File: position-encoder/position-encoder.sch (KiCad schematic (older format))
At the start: 9 parts, among them J1 Conn_01x04_Male, U1 TLE4905L, U2 TLE4905L

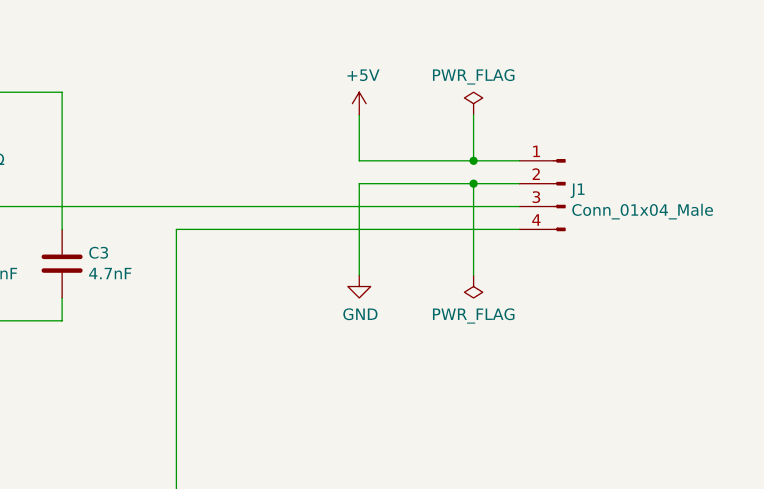
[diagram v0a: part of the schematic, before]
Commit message: Add PCB for position encoder
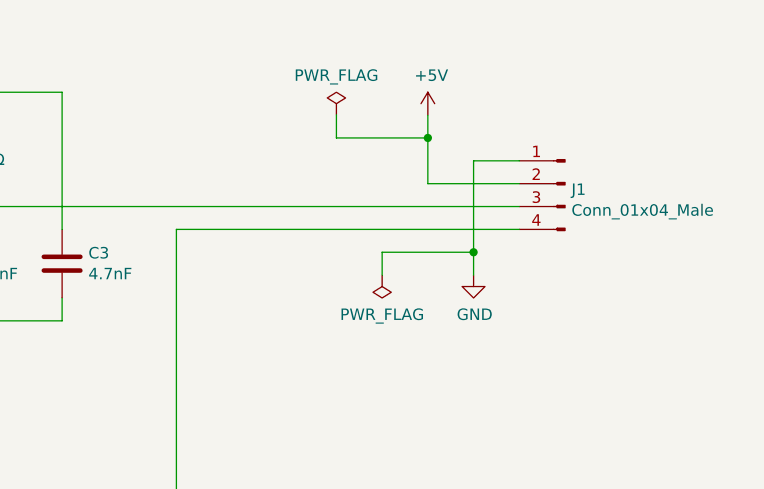
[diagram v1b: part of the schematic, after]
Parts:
- U1, U2: footprint (none) -> earth-rover-custom-footprints:PG-SSO-3-2_W2.54mm_Horizontal_Down
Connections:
- net +5V: now also J1.2 (Pin_2); no longer J1.1 (Pin_1)
- net GND: now also J1.1 (Pin_1); no longer J1.2 (Pin_2)
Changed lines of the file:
@@
 encoding utf-8
 Sheet 1 1
-Title "Position Encoder for RC Volvo C202"
+Title "Position Encoder for Earth Rover"
 Date "2019-11-11"
 Rev "1"
@@
 F 0 "U1" H 2473 3046 50  0000 R CNN
 F 1 "TLE4905L" H 2473 2955 50  0000 R CNN
-F 2 "" H 2700 3000 50  0001 C CNN
+F 2 "earth-rover-custom-footprints:PG-SSO-3-2_W2.54mm_Horizontal_Down" H 2700 3000 50  0001 C CNN
 F 3 "https://www.infineon.com/cms/en/product/sensor/magnetic-sensors/magnetic-position-sensors/hall-switches/tle4905l/" H 2700 3000 50  0001 C CNN
 	1    2700 3000
@@
 F 0 "U2" H 2473 5046 50  0000 R CNN
 F 1 "TLE4905L" H 2473 4955 50  0000 R CNN
-F 2 "" H 2700 5000 50  0001 C CNN
+F 2 "earth-rover-custom-footprints:PG-SSO-3-2_W2.54mm_Horizontal_Down" H 2700 5000 50  0001 C CNN
 F 3 "https://www.infineon.com/cms/en/product/sensor/magnetic-sensors/magnetic-position-sensors/hall-switches/tle4905l/" H 2700 5000 50  0001 C CNN
 	1    2700 5000
@@
 L power:GND #PWR0105
 U 1 1 5DCC09FC
-P 5000 3300
-F 0 "#PWR0105" H 5000 3050 50  0001 C CNN
-F 1 "GND" H 5005 3127 50  0000 C CNN
-F 2 "" H 5000 3300 50  0001 C CNN
-F 3 "" H 5000 3300 50  0001 C CNN
-	1    5000 3300
+P 5500 3300
+F 0 "#PWR0105" H 5500 3050 50  0001 C CNN
+F 1 "GND" H 5505 3127 50  0000 C CNN
+F 2 "" H 5500 3300 50  0001 C CNN
+F 3 "" H 5500 3300 50  0001 C CNN
+	1    5500 3300
 	1    0    0    -1
 $EndComp
@@
 L power:+5V #PWR0106
 U 1 1 5DCC1747
-P 5000 2600
-F 0 "#PWR0106" H 5000 2450 50  0001 C CNN
-F 1 "+5V" H 5015 2773 50  0000 C CNN
-F 2 "" H 5000 2600 50  0001 C CNN
-F 3 "" H 5000 2600 50  0001 C CNN
-	1    5000 2600
+P 5300 2600
+F 0 "#PWR0106" H 5300 2450 50  0001 C CNN
+F 1 "+5V" H 5315 2773 50  0000 C CNN
+F 2 "" H 5300 2600 50  0001 C CNN
+F 3 "" H 5300 2600 50  0001 C CNN
+	1    5300 2600
 	1    0    0    -1
 $EndComp
@@
 L power:PWR_FLAG #FLG0101
 U 1 1 5DD0D13F
-P 5500 2600
-F 0 "#FLG0101" H 5500 2675 50  0001 C CNN
-F 1 "PWR_FLAG" H 5500 2773 50  0000 C CNN
-F 2 "" H 5500 2600 50  0001 C CNN
-F 3 "~" H 5500 2600 50  0001 C CNN
-	1    5500 2600
+P 4900 2600
+F 0 "#FLG0101" H 4900 2675 50  0001 C CNN
+F 1 "PWR_FLAG" H 4900 2773 50  0000 C CNN
+F 2 "" H 4900 2600 50  0001 C CNN
+F 3 "~" H 4900 2600 50  0001 C CNN
+	1    4900 2600
 	1    0    0    -1
 $EndComp
@@
 L power:PWR_FLAG #FLG0102
 U 1 1 5DD0E731
-P 5500 3300
-F 0 "#FLG0102" H 5500 3375 50  0001 C CNN
-F 1 "PWR_FLAG" H 5500 3473 50  0000 C CNN
-F 2 "" H 5500 3300 50  0001 C CNN
-F 3 "~" H 5500 3300 50  0001 C CNN
-	1    5500 3300
+P 5100 3300
+F 0 "#FLG0102" H 5100 3375 50  0001 C CNN
+F 1 "PWR_FLAG" H 5100 3473 50  0000 C CNN
+F 2 "" H 5100 3300 50  0001 C CNN
+F 3 "~" H 5100 3300 50  0001 C CNN
+	1    5100 3300
 	1    0    0    1
 $EndComp
@@
 	4200 3100 5700 3100
 Wire Wire Line
-	5000 3300 5000 2900
-Wire Wire Line
-	5000 2900 5500 2900
-Wire Wire Line
-	5000 2600 5000 2800
-Wire Wire Line
-	5000 2800 5500 2800
-Wire Wire Line
-	5500 2600 5500 2800
-Connection ~ 5500 2800
-Wire Wire Line
-	5500 2800 5700 2800
-Wire Wire Line
-	5500 3300 5500 2900
-Connection ~ 5500 2900
-Wire Wire Line
-	5500 2900 5700 2900
+	5700 2800 5500 2800
+Wire Wire Line
+	5500 2800 5500 3200
+Wire Wire Line
+	5100 3300 5100 3200
+Wire Wire Line
+	5100 3200 5500 3200
+Connection ~ 5500 3200
+Wire Wire Line
+	5500 3200 5500 3300
+Wire Wire Line
+	5300 2600 5300 2700
+Wire Wire Line
+	5300 2900 5700 2900
+Wire Wire Line
+	4900 2600 4900 2700
+Wire Wire Line
+	4900 2700 5300 2700
+Connection ~ 5300 2700
+Wire Wire Line
+	5300 2700 5300 2900
 $EndSCHEMATC

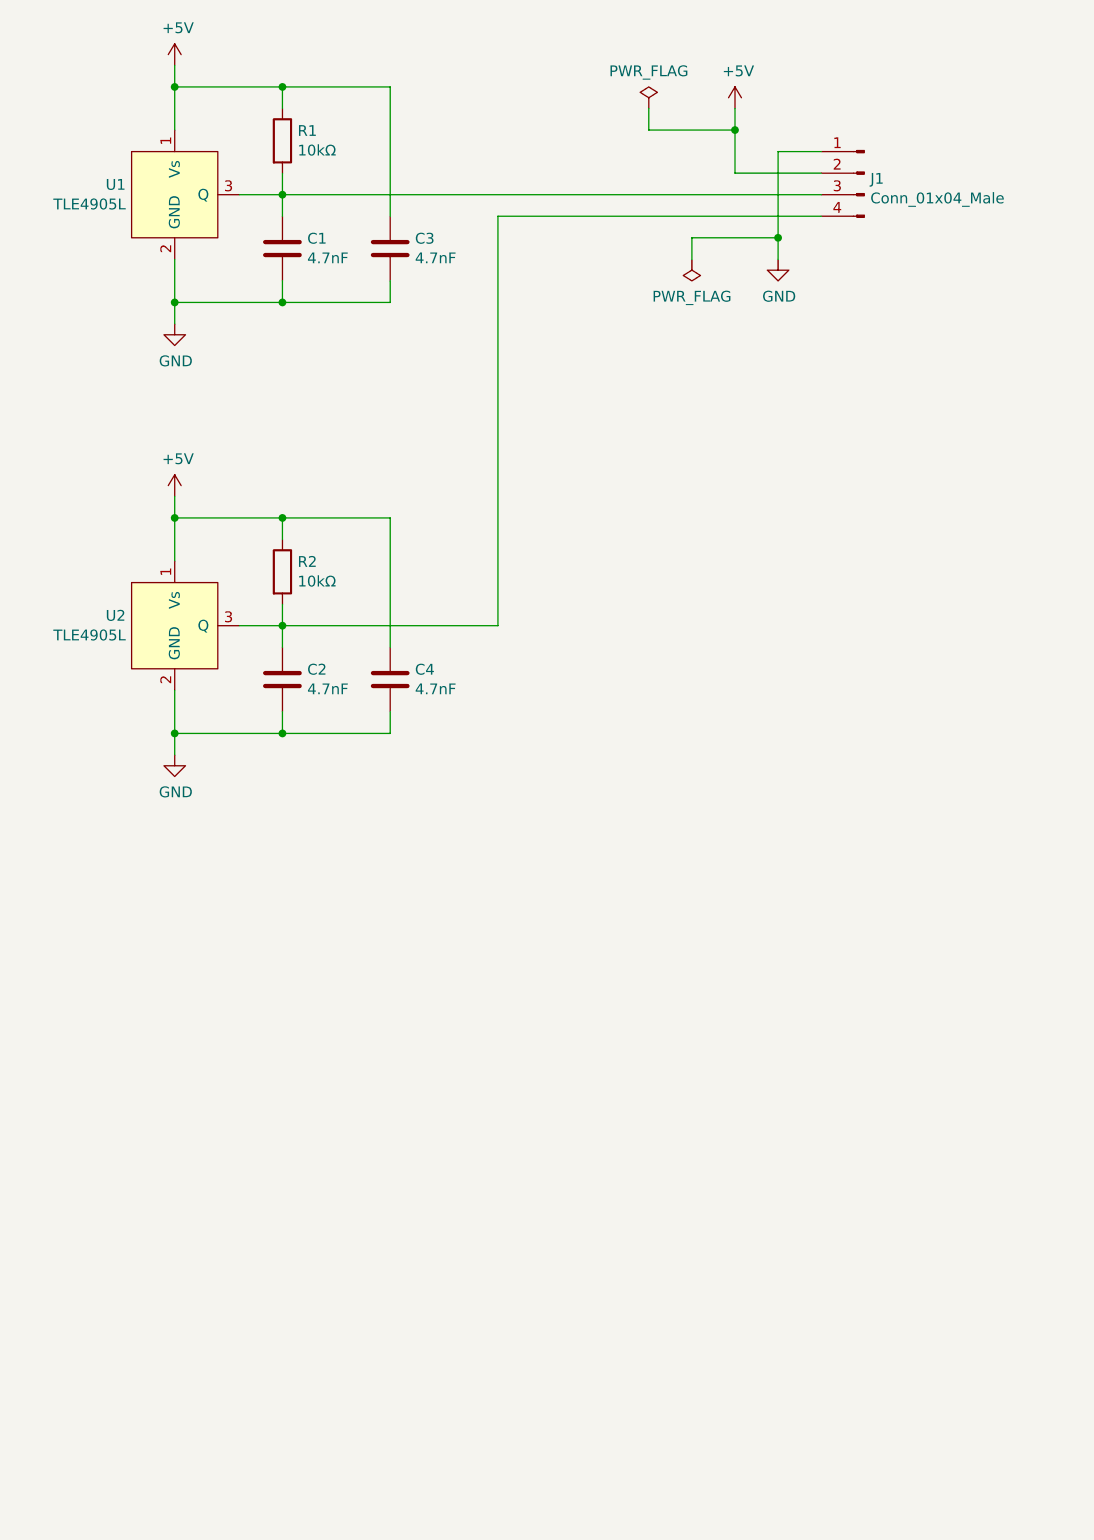
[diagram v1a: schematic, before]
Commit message: Add custom KiCad page layout
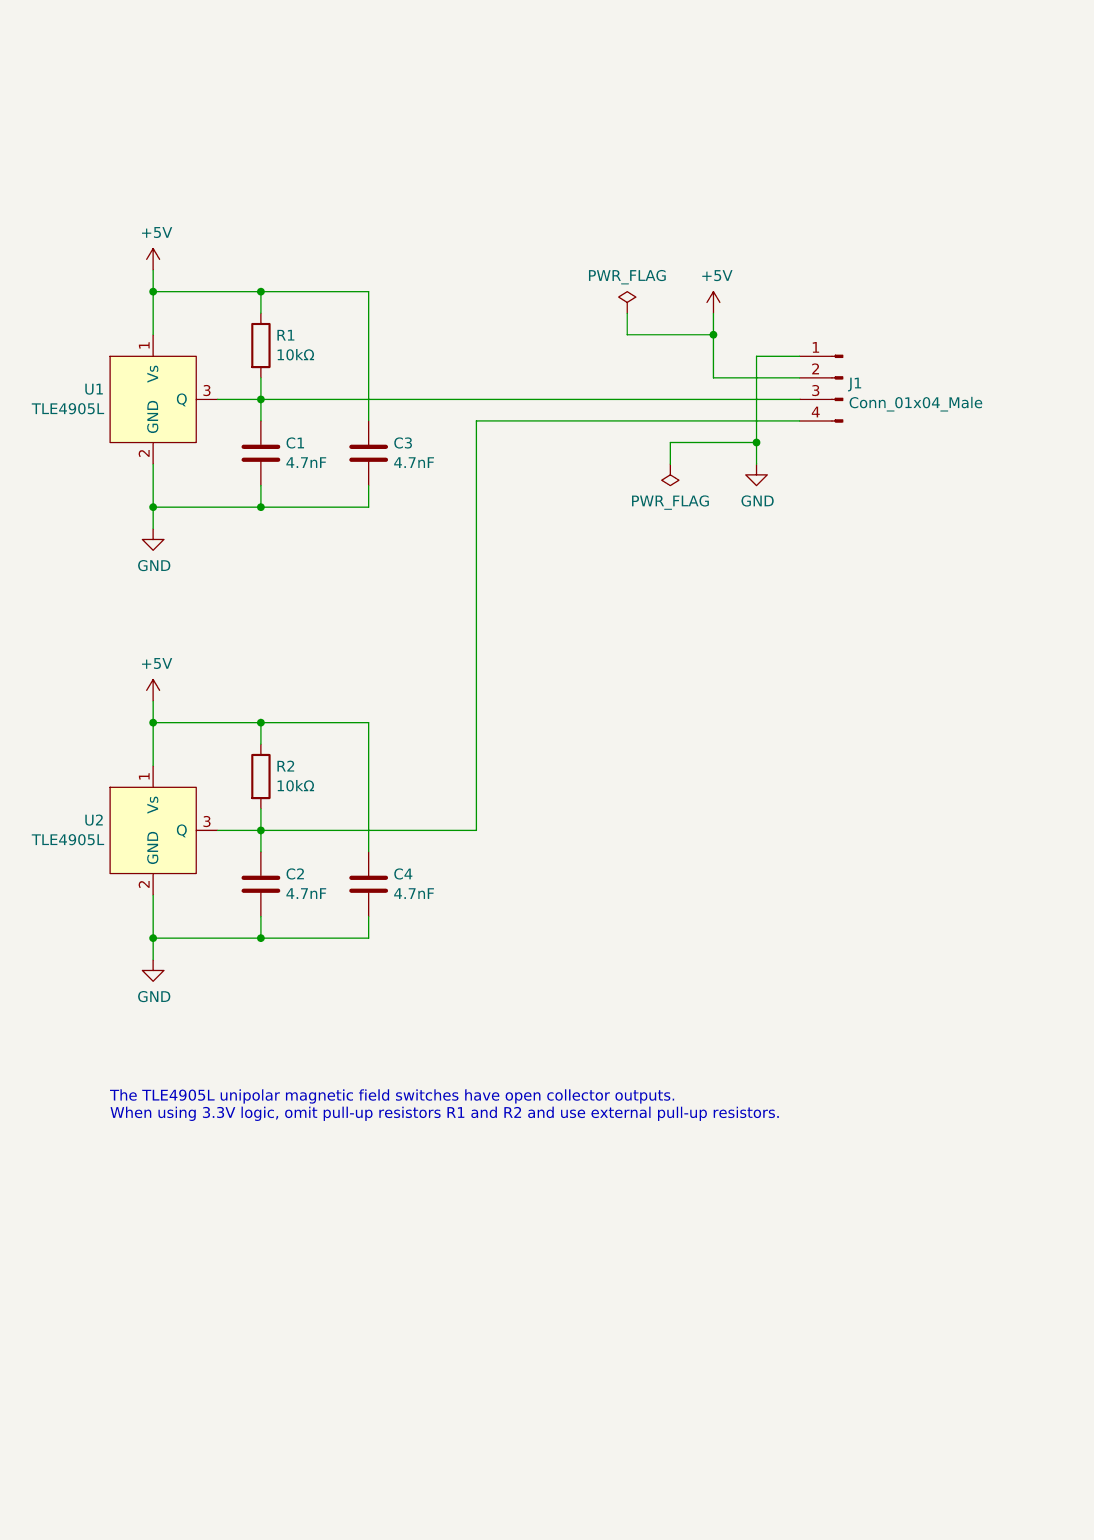
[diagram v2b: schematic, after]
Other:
- note added: "The TLE4905L unipolar magnetic field switches have open collector outputs.\nWhen using 3.3V logic, omit pull-up resistors R1 and R2 and use external pull-up resistors."
- moved on the sheet: C1, C2, C3, C4, J1, R1, R2, U1, U2

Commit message: Improve layouts and add capacitors
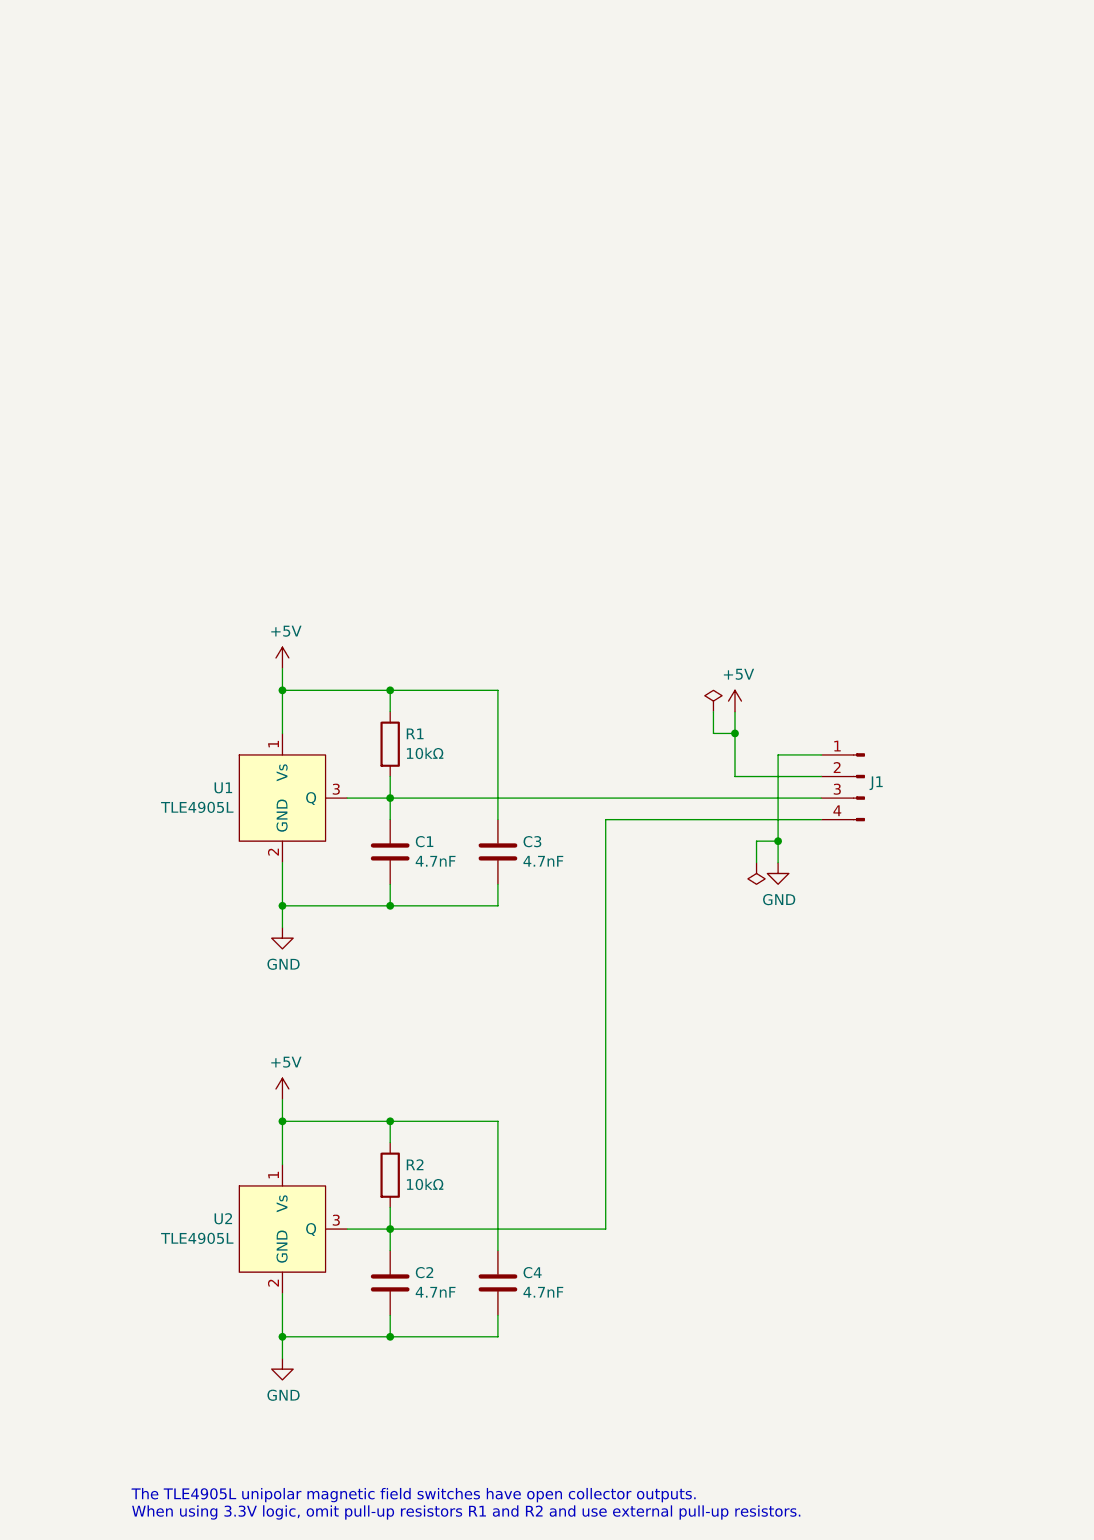
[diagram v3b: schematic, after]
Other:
- moved on the sheet: C1, C2, C3, C4, J1, R1, R2, U1, U2

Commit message: Review schematics
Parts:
- R1, R2: value 10kΩ -> 10k(*)
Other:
- note added: "(*) The TLE4905L unipolar magnetic field switches have open collector outputs.\nWhen using 3.3V logic, omit pull-up resistors R1 and R2 and use external pull-up resistors."
- note removed: "The TLE4905L unipolar magnetic field switches have open collector outputs.\nWhen using 3.3V logic, omit pull-up resistors R1 and R2 and use external pull-up resistors."
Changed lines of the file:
@@
 EESchema Schematic File Version 4
-LIBS:position-encoder-cache
 EELAYER 30 0
 EELAYER END
@@
 P 3700 7550
 F 0 "R2" H 3770 7596 50  0000 L CNN
-F 1 "10kΩ" H 3770 7505 50  0000 L CNN
+F 1 "10k(*)" H 3770 7505 50  0000 L CNN
 F 2 "Resistor_THT:R_Axial_DIN0207_L6.3mm_D2.5mm_P7.62mm_Horizontal" V 3630 7550 50  0001 C CNN
 F 3 "~" H 3700 7550 50  0001 C CNN
@@
 P 3700 5550
 F 0 "R1" H 3770 5596 50  0000 L CNN
-F 1 "10kΩ" H 3770 5505 50  0000 L CNN
+F 1 "10k(*)" H 3770 5505 50  0000 L CNN
 F 2 "Resistor_THT:R_Axial_DIN0207_L6.3mm_D2.5mm_P7.62mm_Horizontal" V 3630 5550 50  0001 C CNN
 F 3 "~" H 3700 5550 50  0001 C CNN
@@
 	5300 5500 5300 5700
 Text Notes 2500 9150 0    50   ~ 0
-The TLE4905L unipolar magnetic field switches have open collector outputs.\nWhen using 3.3V logic, omit pull-up resistors R1 and R2 and use external pull-up resistors.
+(*) The TLE4905L unipolar magnetic field switches have open collector outputs.\nWhen using 3.3V logic, omit pull-up resistors R1 and R2 and use external pull-up resistors.
 $EndSCHEMATC
